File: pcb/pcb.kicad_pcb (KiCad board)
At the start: 2 copper layers, 117 x 96 mm, 50 parts, among them J1 BATT, J2 BATT, SW1 SW_SPST, SW10 SW_SPST, SW11 SW_SPST, SW12 SW_SPST, SW13 SW_SPST, SW14 SW_SPST, SW15 SW_SPST, SW16 SW_SPST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

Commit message: add ci and 3d files
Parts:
- D1, D10, D11, D12, D13, D14, D15, D16, D17, D18, D2, D3, D4, D5, D6, D7, D8, D9: footprint scuffy:Diode_TH_SMD_DUAL -> one-s:Diode_TH_SMD_DUAL
- G1, G2: footprint scuffy:OSHW-logo -> one-s:OSHW-logo
- H1, H2, H3, H4: footprint scuffy:Hole_4.2mm -> one-s:Hole_4.2mm
- H5, H6, H7: footprint scuffy:Hole_2.2mm -> one-s:Hole_2.2mm
- J1: footprint scuffy:JST_SH_Battery_DUAL -> one-s:JST_SH_Battery_DUAL; moved to F.Cu
- J2: footprint scuffy:Battery -> one-s:Battery
- PWR1: footprint scuffy:MSK-12C02_DUAL -> one-s:MSK-12C02_DUAL
- SW1, SW10, SW11, SW12, SW13, SW14, SW15, SW16, SW17, SW18, SW2, SW3, SW4, SW5, SW6, SW7, SW8, SW9: footprint scuffy:KS-27_KS-33_Hotswap_1U_DUAL -> one-s:KS-27_KS-33_Hotswap_1U_DUAL
- U1: footprint scuffy:XIAO_nRF52840_DUAL -> one-s:XIAO_nRF52840_DUAL
- turned J1 to -90 degrees

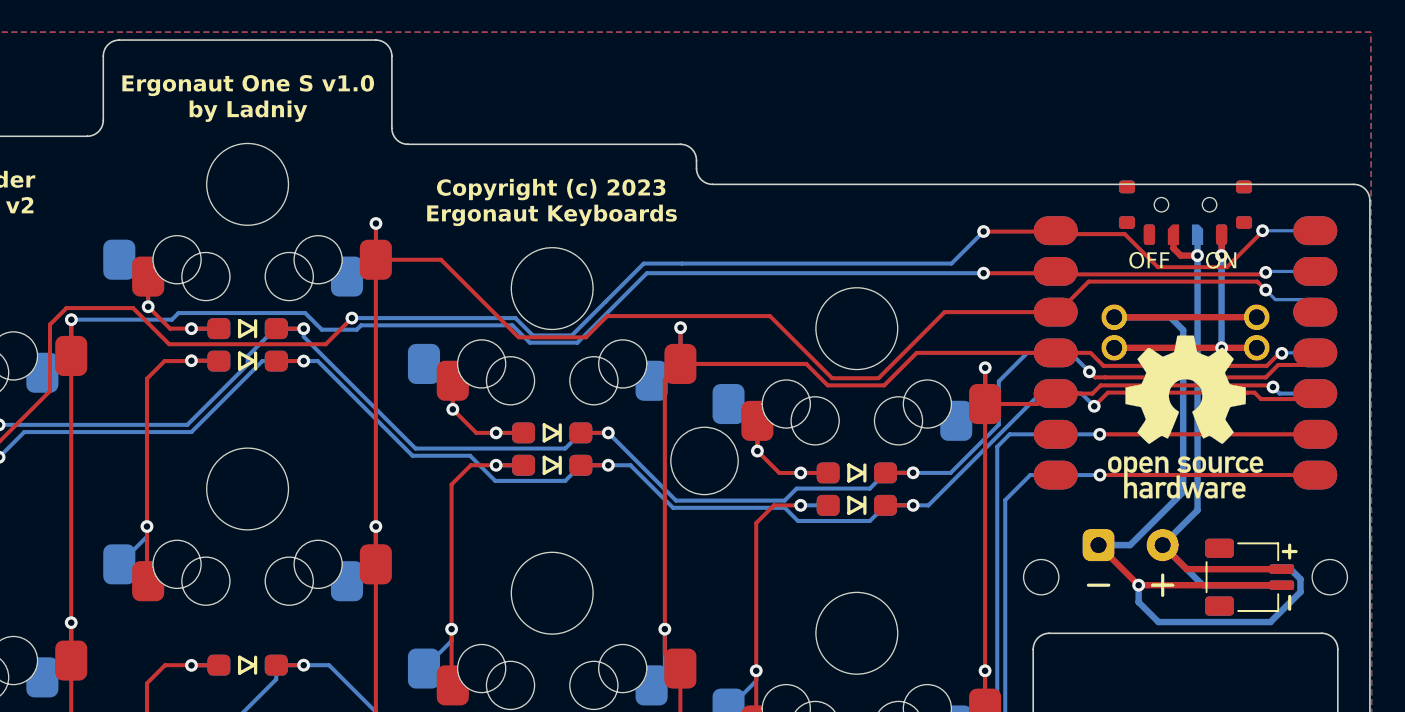
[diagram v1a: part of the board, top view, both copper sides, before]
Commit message: Round and enlarge xiao pads, add cutout under controller
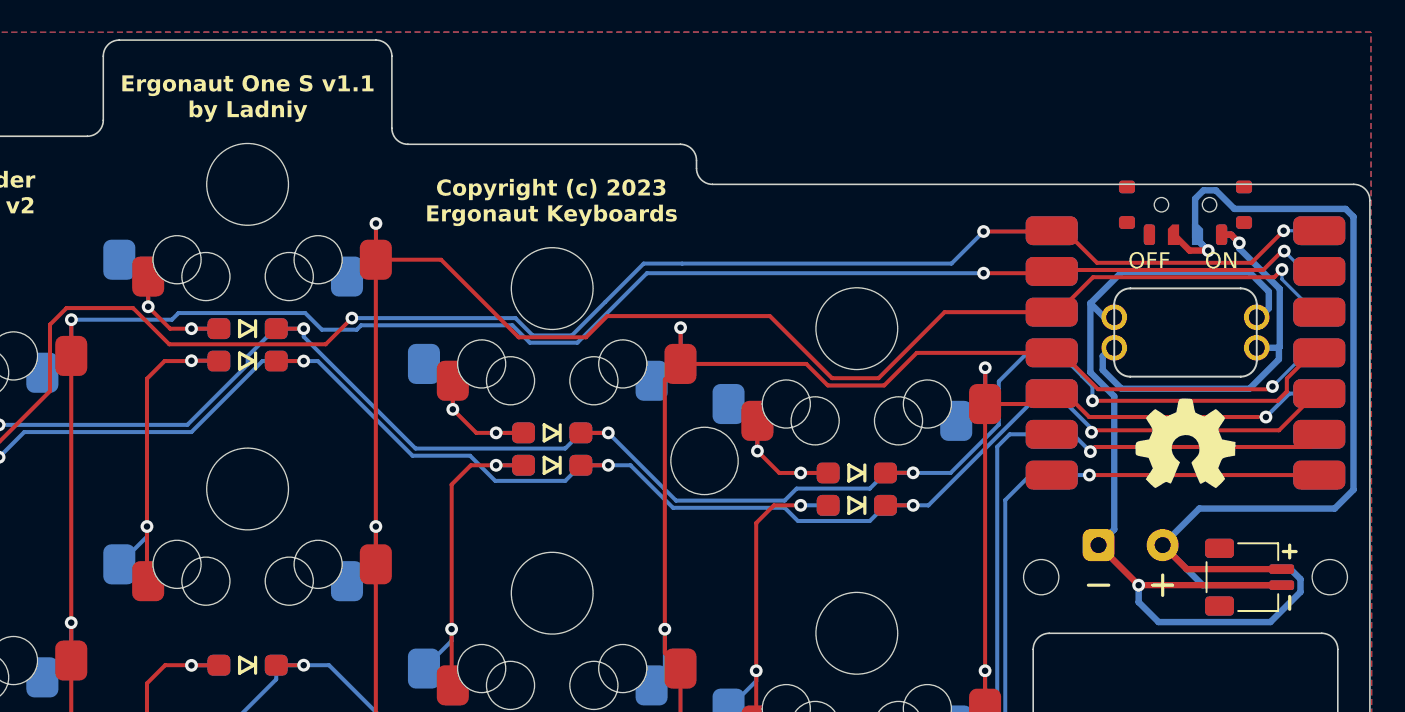
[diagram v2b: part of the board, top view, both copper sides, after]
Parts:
- removed G1, G2: LOGO, one-s:OSHW-logo
- added G***: LOGO, LOGO, F.Cu at (190.4, 80.4)
- added G***: LOGO, LOGO, B.Cu at (190.4, 80.4)
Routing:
- net Net-(J1-Pin_1): track 39.3 -> 65.0 mm
- net B+: track 17.2 -> 26.0 mm, vias 2 -> 1
- net R0: track 132.6 -> 134.8 mm
- net B-: track 57.7 -> 59.5 mm
- net C3: track 133.5 -> 134.8 mm
- net R1: track 128.6 -> 129.7 mm
- net C2: track 155.8 -> 156.8 mm
- net C1: track 133.9 -> 134.8 mm
- net R2: track 145.8 -> 146.7 mm
- net C4: track 118.9 -> 119.7 mm
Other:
- board text added: "Ergonaut One S v1.1 by Ladniy"
- board text removed: "Ergonaut One S v1.0 by Ladniy"

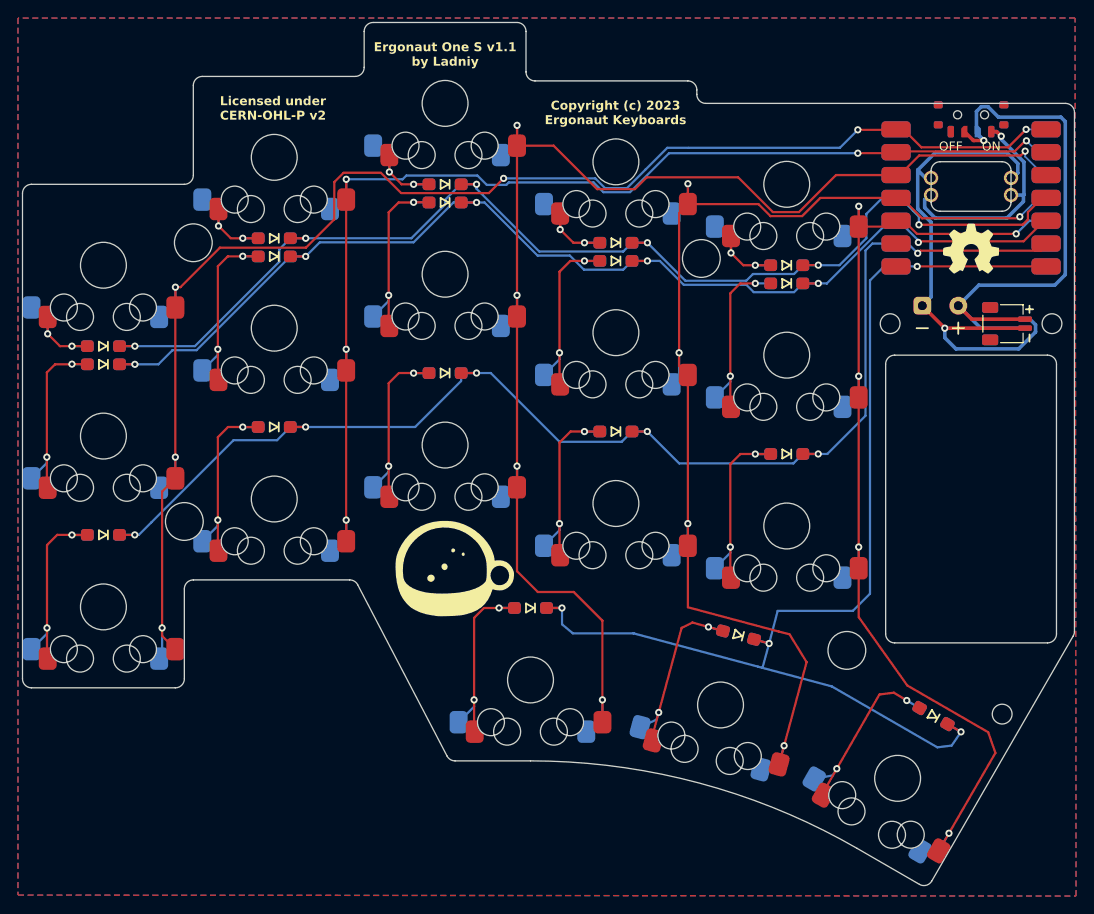
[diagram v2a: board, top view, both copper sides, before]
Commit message: Modify PCB for Kailh P1316S
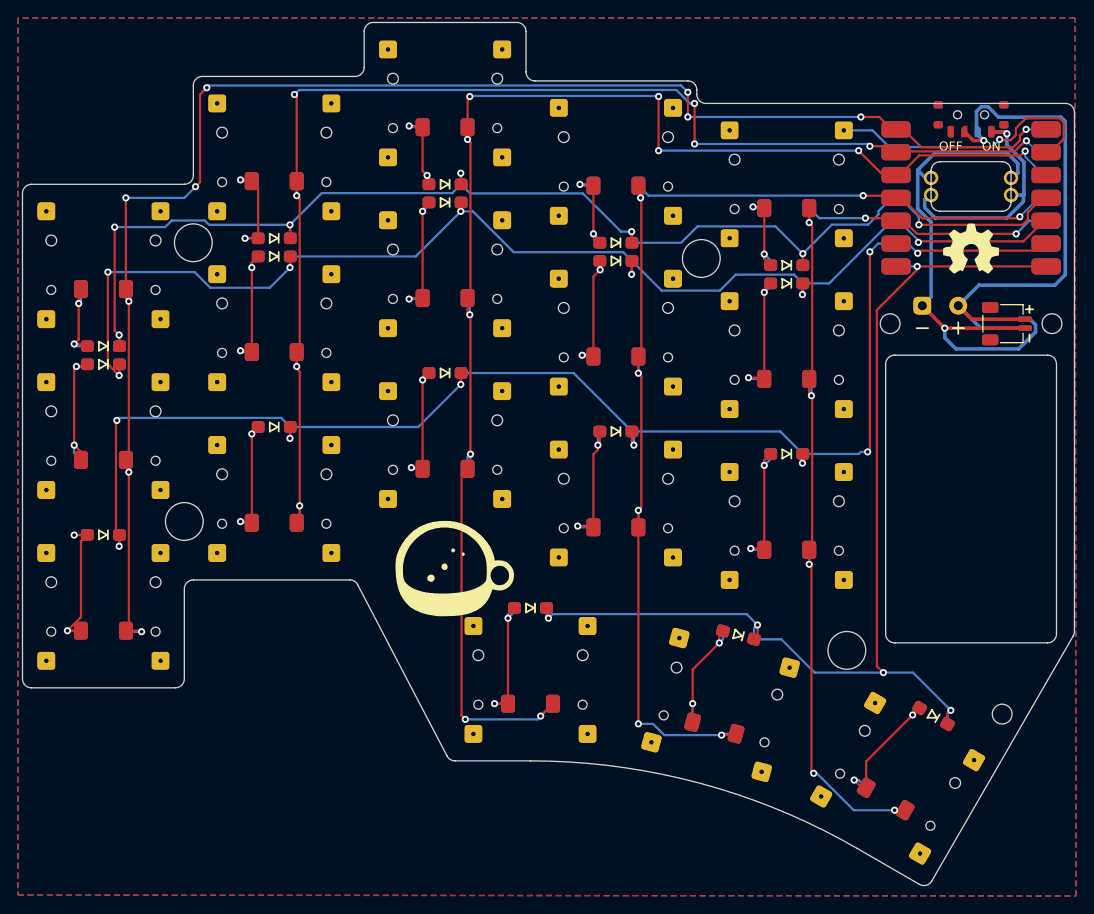
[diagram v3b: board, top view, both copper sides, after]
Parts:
- SW1, SW10, SW11, SW12, SW13, SW14, SW15, SW16, SW17, SW18, SW2, SW3, SW4, SW5, SW6, SW7, SW8, SW9: footprint one-s:KS-27_KS-33_Hotswap_1U_DUAL -> one-s:CPG1316S01D02_REV
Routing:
- net GND: track 0.00 -> 31.8 mm, vias 0 -> 1
- net R1: track 129.7 -> 142.9 mm, vias 6 -> 7
- net R2: track 146.7 -> 158.9 mm, vias 6 -> 9
- net C0: track 164.4 -> 174.1 mm, vias 6 -> 10
- net C1: track 134.8 -> 144.0 mm, vias 5 -> 8
- net R3: track 133.3 -> 124.0 mm, vias 4 -> 5
- net Net-(D13-A): track 22.4 -> 13.6 mm
- net C4: track 119.7 -> 110.9 mm, vias 5 -> 7
- net C3: track 134.8 -> 126.5 mm, vias 5 -> 7
- net R0: track 134.8 -> 143.0 mm, vias 6 -> 7
- net Net-(D9-A): track 22.4 -> 14.6 mm
- net Net-(D12-A): track 22.4 -> 14.6 mm
- net Net-(D7-A): track 22.4 -> 15.1 mm
- net Net-(D17-A): track 22.3 -> 15.1 mm
- net Net-(D6-A): track 22.6 -> 15.4 mm
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- added copper zone on B.Cu, net GND
- added copper zone on F.Cu, net GND
- removed copper zone on B.Cu, net (none)
- removed copper zone on F.Cu, net (none)
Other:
- board text removed: "Copyright (c) 2023 Ergonaut Keyboards"
- board text removed: "Ergonaut One S v1.1 by Ladniy"
- board text removed: "Licensed under CERN-OHL-P v2"
